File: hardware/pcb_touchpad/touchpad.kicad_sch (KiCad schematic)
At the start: 23 parts

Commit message: created iqs9151 symbol
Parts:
- added U1: IQS9151, Package_DFN_QFN:VQFN-52-1EP_6x6mm_P0.4mm_EP4.7x4.7mm, symbol IQS9151:IQS9151
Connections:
- net at ROW7.P1: now also U1.44 (TX37)
- net at COL10.P1: now also U1.29 (RX9/TX9)
- net at ROW2.P1: now also U1.36 (RX12/TX12)
- net at ROW11.P1: now also U1.48 (TX41)
- net at COL9.P1: now also U1.26 (RX8/TX8)
- net at COL3.P1: now also U1.11 (RX2/TX2)
- net at COL5.P1: now also U1.16 (RX4/TX4)
- net at ROW8.P1: now also U1.45 (TX38)
- net at ROW6.P1: now also U1.43 (TX36)
- net at COL8.P1: now also U1.24 (RX7/TX7)
- net at ROW10.P1: now also U1.47 (TX40)
- net at COL7.P1: now also U1.21 (RX6/TX6)
- net at ROW1.P1: now also U1.34 (RX11/TX11)
- net at ROW9.P1: now also U1.46 (TX39)
- net at COL4.P1: now also U1.14 (RX3/TX3)
- net at ROW13.P1: now also U1.50 (TX43)
- net at ROW3.P1: now also U1.40 (TX33)
- net at ROW5.P1: now also U1.42 (TX35)
- net at ROW12.P1: now also U1.49 (TX42)
- net at ROW4.P1: now also U1.41 (TX34)
- net at COL1.P1: now also U1.6 (RX0/TX0)
- net at COL2.P1: now also U1.8 (RX1/TX1)
- net at COL6.P1: now also U1.19 (RX5/TX5)
- new net: U1.37 (NC), U1.38 (NC)
- new net GND: U1.3 (VSS)
- no-connect marks 0 -> 2
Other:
- moved on the sheet: COL1, COL10, COL2, COL3, COL4, COL5, COL6, COL7, COL8, COL9, ROW1, ROW10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

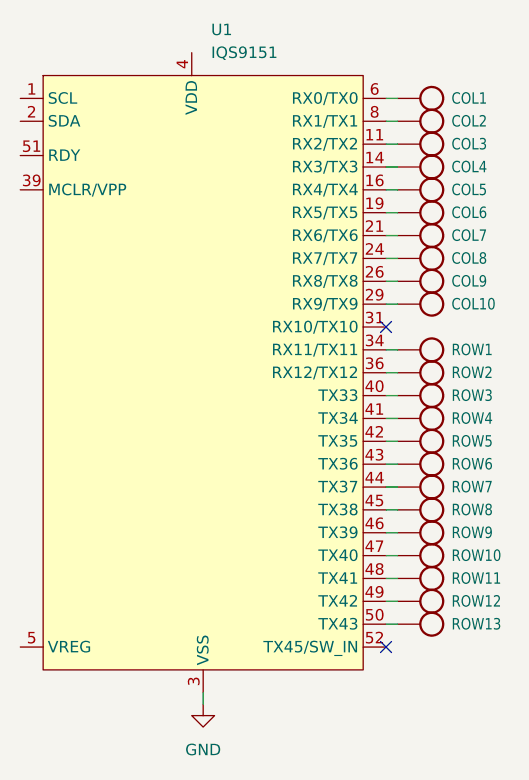
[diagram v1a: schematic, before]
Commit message: modified QFN footprint of IQS9151
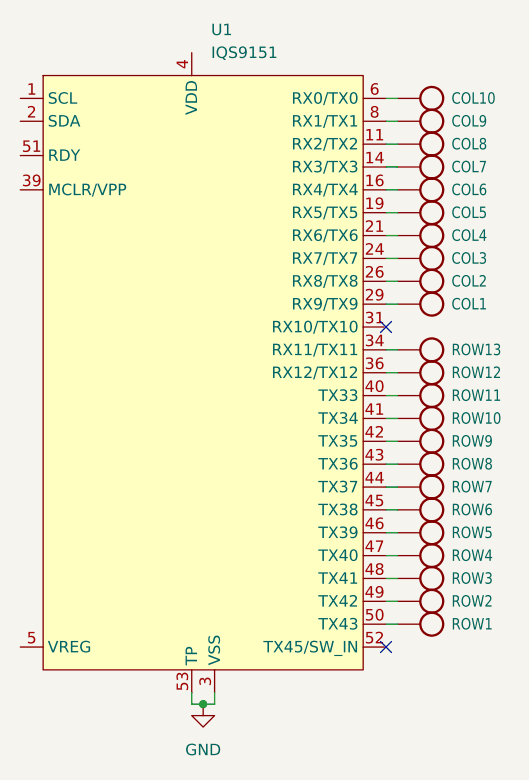
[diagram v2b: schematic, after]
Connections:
- net GND: now also U1.53 (TP)
- net at COL10.P1: now also U1.6 (RX0/TX0); no longer U1.29 (RX9/TX9)
- net at ROW2.P1: now also U1.49 (TX42); no longer U1.36 (RX12/TX12)
- net at ROW11.P1: now also U1.40 (TX33); no longer U1.48 (TX41)
- net at COL9.P1: now also U1.8 (RX1/TX1); no longer U1.26 (RX8/TX8)
- net at COL3.P1: now also U1.24 (RX7/TX7); no longer U1.11 (RX2/TX2)
- net at COL5.P1: now also U1.19 (RX5/TX5); no longer U1.16 (RX4/TX4)
- net at ROW8.P1: now also U1.43 (TX36); no longer U1.45 (TX38)
- net at ROW6.P1: now also U1.45 (TX38); no longer U1.43 (TX36)
- net at COL8.P1: now also U1.11 (RX2/TX2); no longer U1.24 (RX7/TX7)
- net at ROW10.P1: now also U1.41 (TX34); no longer U1.47 (TX40)
- net at COL7.P1: now also U1.14 (RX3/TX3); no longer U1.21 (RX6/TX6)
- net at ROW1.P1: now also U1.50 (TX43); no longer U1.34 (RX11/TX11)
- net at ROW9.P1: now also U1.42 (TX35); no longer U1.46 (TX39)
- net at COL4.P1: now also U1.21 (RX6/TX6); no longer U1.14 (RX3/TX3)
- net at ROW13.P1: now also U1.34 (RX11/TX11); no longer U1.50 (TX43)
- net at ROW3.P1: now also U1.48 (TX41); no longer U1.40 (TX33)
- net at ROW5.P1: now also U1.46 (TX39); no longer U1.42 (TX35)
- net at ROW12.P1: now also U1.36 (RX12/TX12); no longer U1.49 (TX42)
- net at ROW4.P1: now also U1.47 (TX40); no longer U1.41 (TX34)
- net at COL1.P1: now also U1.29 (RX9/TX9); no longer U1.6 (RX0/TX0)
- net at COL2.P1: now also U1.26 (RX8/TX8); no longer U1.8 (RX1/TX1)
- net at COL6.P1: now also U1.16 (RX4/TX4); no longer U1.19 (RX5/TX5)
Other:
- moved on the sheet: COL1, COL10, COL2, COL3, COL4, COL5, COL6, COL7, COL8, COL9, ROW1, ROW10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
